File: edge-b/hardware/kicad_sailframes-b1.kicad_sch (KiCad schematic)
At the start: 0 parts

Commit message: B1 schematic Section 8: Battery Monitor (proof of concept)
3 components: R1 (100k), R2 (100k), C1 (100nF). 6 wire stubs, 6 net
labels (VBAT x1, VBAT_DIV x3, GND x2). Verified to open cleanly in
KiCad 10.

Pattern: use Device:R and Device:C from KiCad's standard Device library
(symbol defs copied into the schematic's lib_symbols section), place
each component with a fresh UUID, give each pin a short wire stub to a
named label. Matching labels create electrical connections without
needing junctions or drawn wires between components. ERC will flag
single-occurrence labels until the connecting section is added — e.g.,
VBAT is 1x here, will become 2x when TP4056 BAT pin is added in Section
1.

Library symbol Device:R copied verbatim from edge-e/hardware/kicad_sailframes-e1.kicad_sch
(already at 2-tab indent and named "Device:R"). Library symbol Device:C
copied from KiCad's bundled Device.kicad_sym with +1 tab adjustment and
"C" -> "Device:C" rename on the first line. Both are KiCad-10 format.

Build script lives at /tmp/build_section8.py for reference. Sections 2,
10, 1 will follow the same pattern with components from the project
libraries (B1_MT3608, B1_JLC, etc.) — verifying actual symbol names
before referencing.

Co-Authored-By: Claude Opus 4.7 (1M context) <noreply@anthropic.com>
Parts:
- added C1: 100nF, Capacitor_SMD:C_0603_1608Metric, symbol Device:C
- added R1, R2: 100k, Resistor_SMD:R_0603_1608Metric, symbol Device:R
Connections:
- new net GND: C1.2, R2.2
- new net VBAT: R1.1
- new net VBAT_DIV: C1.1, R1.2, R2.1

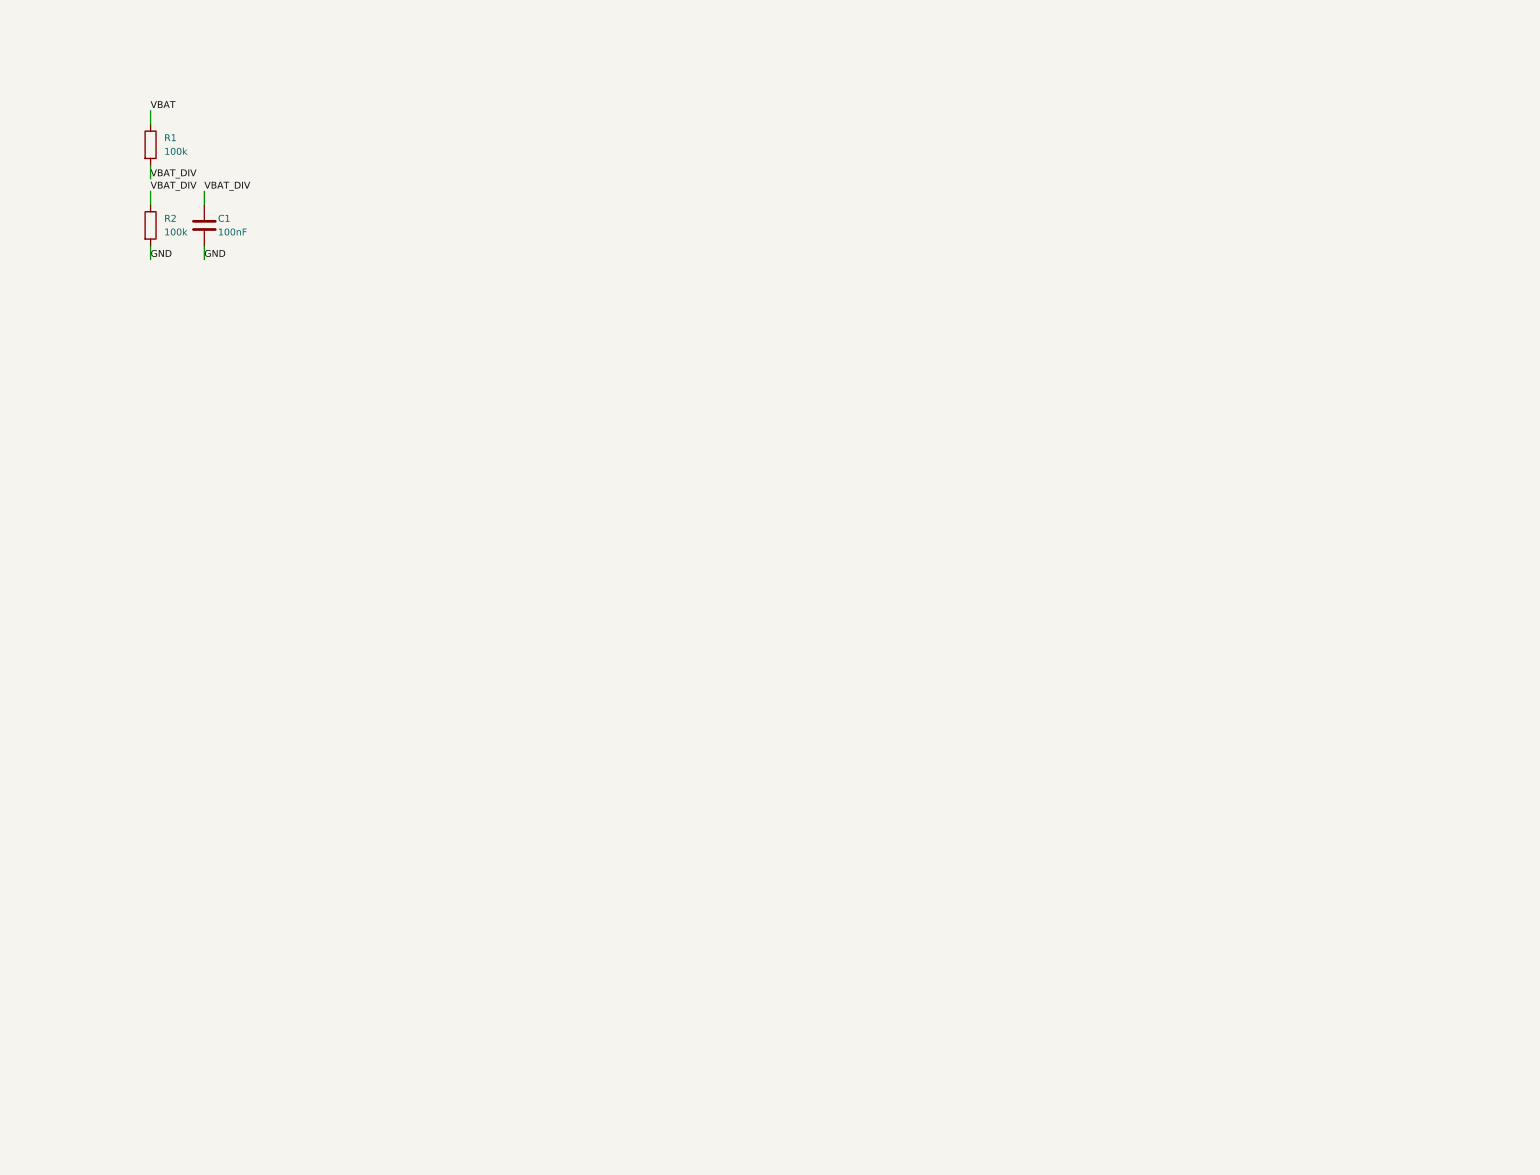
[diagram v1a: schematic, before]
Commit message: B1 schematic Sections 1+2+8+10: power, boost, battery monitor, Hall latch
32 new components + 85 wires + 85 labels added on top of Section 8's
baseline (3 components, 6 wires, 6 labels). Total now 35 / 91 / 91.

Section 1 (Power Input + Charger): U2 TP4056 SOIC-8, D7/D8 SS14 OR-ing
diodes, D2 yellow + D3 green LEDs (CHRG/STDBY indicators) with R8/R9
series 1k, R6 (PROG 2k) and R7 (TEMP 10k), C2/C3 VCC decoupling (10uF +
100nF), C4/C5 BAT decoupling (10uF + 100nF), J2 JST PH for battery,
J_QI 2-pin Qi solder pads.

Section 2 (Boost Converter): U3 MT3608 SOT-23-6, L1 22uH inductor, D9
SS14 boost diode, C7 10uF input cap, C8 22uF output cap, R10/R11 100k
/ 13.3k feedback divider (Vout ~5.11V, can refine to 13.7k for 4.98V).
MT3608 EN pin nets to LATCH_Q (spec checklist line 1259 - the
double-gating requirement). MT3608 NC pin (6) marked no_connect.

Section 10 (Hall Latch / Magnetic Power Switch): U_HALL DRV5032AJ, R12
100k pull-up for open-drain, R13/C9 10k/100nF debounce, U_FF
SN74LVC1G74DCTR SM8 flip-flop in toggle config (D tied to /Q via
FF_D_QBAR label), U_RST MAX809T 3.08V supervisor on /CLR (spec
checklist line 1260 - no RC POR network), R14 10k base resistor, Q_INV
2N3904 NPN level shifter, R15 100k gate pull-up, Q_PWR AO3401A P-MOSFET
switching V5_UNSW to V5_SW. U_HALL pin 3 (NC per symbol) marked
no_connect.

Library additions to lib_symbols (8 new top-level): Device:C, Device:L,
Device:LED, Connector_Generic:Conn_01x02, B1_TP4056:TP4056,
B1_MT3608:MT3608, B1_SS14:SS14, B1_DRV5032AJ:DRV5032AJDMRR,
B1_2N3904:MMBT3904-C20526, B1_AO3401A:AO3401A,
B1_JLC:SN74LVC1G74DCTR, B1_JLC:MAX809T.

Net distribution:
- GND: 22, VBAT: 12 (high-fanout rails)
- TP4056_VCC: 6 (VCC + CE + 2 decoupling caps + OR-diodes' cathodes)
- V5_UNSW: 5, V5_SW: 4 (pre/post Q_PWR MOSFET)
- LATCH_Q: 3 (U_FF.Q + R14 + MT3608.EN - the critical double-gate)
- Internal section nets (HALL_OUT, CLK_DEBOUNCED, FB_MID, etc.): 2-3 each

Verified to load cleanly in KiCad 10 after stripping ; comments (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
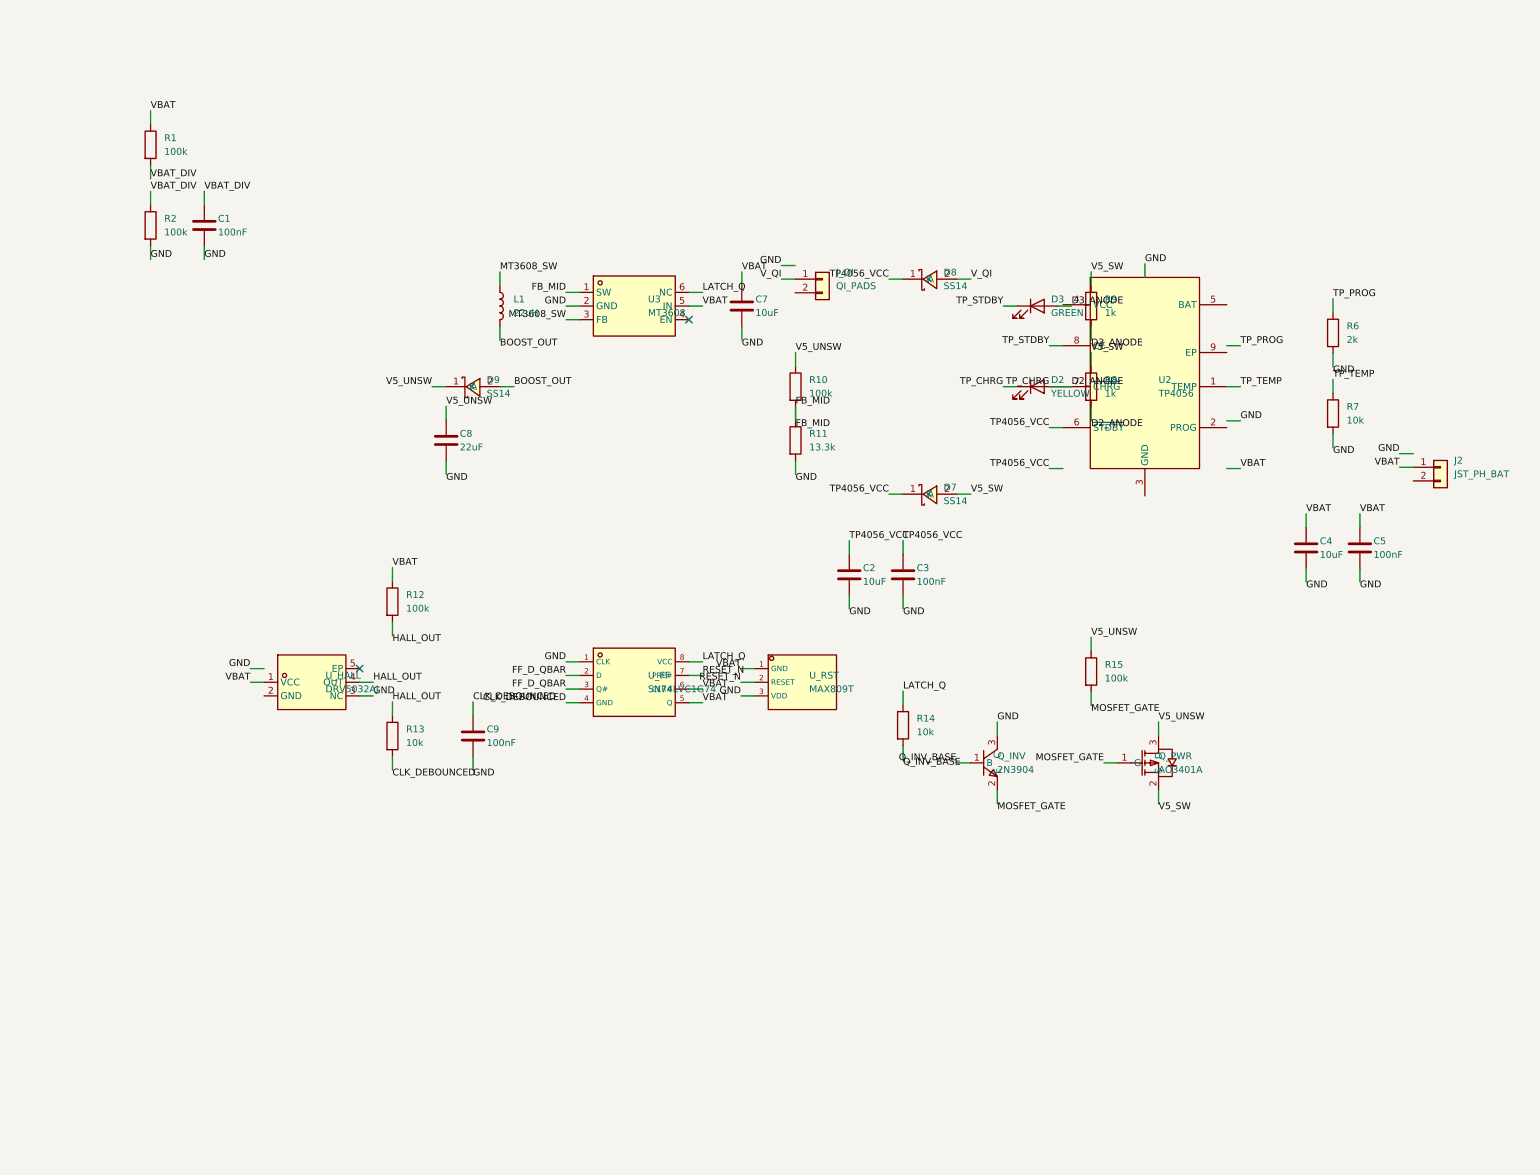
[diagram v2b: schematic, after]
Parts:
- added C2, C4, C7: 10uF, Capacitor_SMD:C_0603_1608Metric, symbol Device:C
- added C3, C5, C9: 100nF, Capacitor_SMD:C_0603_1608Metric, symbol Device:C
- added C8: 22uF, Capacitor_SMD:C_0603_1608Metric, symbol Device:C
- added D2: YELLOW, LED_SMD:LED_0805_2012Metric, symbol Device:LED
- added D3: GREEN, LED_SMD:LED_0805_2012Metric, symbol Device:LED
- added D7, D8, D9: SS14, Diode_SMD:D_SMA, symbol B1_SS14:SS14
- added J2: JST_PH_BAT, Connector_JST:JST_PH_S2B-PH-K_1x02_P2.00mm_Vertical, symbol Connector_Generic:Conn_01x02
- added J_QI: QI_PADS, Connector_PinHeader_2.54mm:PinHeader_1x02_P2.54mm_Vertical, symbol Connector_Generic:Conn_01x02
- added L1: 22uH, Inductor_SMD:L_Bourns_SRR4528, symbol Device:L
- added Q_INV: 2N3904, Package_TO_SOT_SMD:SOT-23, symbol B1_2N3904:MMBT3904-C20526
- added Q_PWR: AO3401A, Package_TO_SOT_SMD:SOT-23, symbol B1_AO3401A:AO3401A
- added R10, R12, R15: 100k, Resistor_SMD:R_0603_1608Metric, symbol Device:R
- added R11: 13.3k, Resistor_SMD:R_0603_1608Metric, symbol Device:R
- added R13, R14, R7: 10k, Resistor_SMD:R_0603_1608Metric, symbol Device:R
- added R6: 2k, Resistor_SMD:R_0603_1608Metric, symbol Device:R
- added R8, R9: 1k, Resistor_SMD:R_0603_1608Metric, symbol Device:R
- added U2: TP4056, Package_SO:SOIC-8_3.9x4.9mm_P1.27mm, symbol B1_TP4056:TP4056
- added U3: MT3608, Package_TO_SOT_SMD:SOT-23-6, symbol B1_MT3608:MT3608
- added U_FF: SN74LVC1G74, Package_SO:SM8, symbol B1_JLC:SN74LVC1G74DCTR
- added U_HALL: DRV5032AJ, Package_DFN_QFN:X2SON-4_1x1mm_P0.5mm, symbol B1_DRV5032AJ:DRV5032AJDMRR
- added U_RST: MAX809T, Package_TO_SOT_SMD:SOT-23, symbol B1_JLC:MAX809T
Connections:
- net GND: now also C2.2, C3.2, C4.2, C5.2, C7.2, C8.2, C9.2, Q_INV.3 (C), R11.2, R6.2, R7.2, U3.2 (GND), U_FF.1 (CLK), U_HALL.3 (NC), U_RST.3 (VDD)
- net VBAT: now also C4.1, C5.1, C7.1, J2.1 (Pin_1), R12.1, U3.5 (IN), U_FF.5 (Q), U_FF.6 (CLR#), U_HALL.1 (VCC), U_RST.1 (GND)
- new net BOOST_OUT: D9.2 (A), L1.2
- new net CLK_DEBOUNCED: C9.1, R13.2, U_FF.4 (GND)
- new net D2_ANODE: D2.1 (K), D2.2 (A), R8.2, U2.7 (~{CHRG})
- new net D3_ANODE: D3.2 (A), R9.2
- new net FB_MID: R10.2, R11.1, U3.1 (SW)
- new net FF_D_QBAR: U_FF.2 (D), U_FF.3 (Q#)
- new net HALL_OUT: R12.2, R13.1, U_HALL.4 (OUT)
- new net LATCH_Q: R14.1, U3.6 (NC), U_FF.8 (VCC)
- new net MOSFET_GATE: Q_INV.2 (E), Q_PWR.1 (G), R15.2
- new net MT3608_SW: L1.1, U3.3 (FB)
- new net Q_INV_BASE: Q_INV.1 (B), R14.2
- new net RESET_N: U_FF.7 (PRE#), U_RST.2 (RESET)
- new net TP4056_VCC: C2.1, C3.1, D7.1 (K), D8.1 (K), U2.6 (~{STDBY})
- new net TP_PROG: R6.1
- new net TP_STDBY: D3.1 (K), U2.8 (CE)
- new net TP_TEMP: R7.1, U2.1 (TEMP)
- new net V5_SW: D7.2 (A), Q_PWR.2 (S), R8.1, R9.1
- new net V5_UNSW: C8.1, D9.1 (K), Q_PWR.3 (D), R10.1, R15.1
- new net V_QI: D8.2 (A), J_QI.1 (Pin_1)
- no-connect marks 0 -> 2

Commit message: B1 schematic ERC cleanup: Y-flip fix, PWR_FLAGs, R11 tuning
Critical bug fix: pin canvas position was computed using sym_y + py
instead of sym_y - py. KiCad symbols use Y-up math convention while
schematic canvas uses Y-down — KiCad inverts Y when placing symbols.
The earlier code missed this. For symmetric components (R, C, L) the
bug only swapped pin 1 with pin 2 — electrically equivalent. For
asymmetric components (TP4056, MT3608, U_FF, U_HALL, ...), wires landed
5–30 mm away from actual pins, leaving 8 pins unconnected.

Fix:
- stub_label() now computes canvas Y as comp_y - py (Y-flip)
- stub_offset() rotations 90 and 270 swapped (pin direction inverts
  with Y axis)
- Section 8 connection data swapped pin 1 ↔ pin 2 to preserve original
  visual (VBAT label above R1, VBAT_DIV between R1↔R2, GND below)

Additional cleanup in this commit:
- 7 PWR_FLAG instances added on each power rail (VBAT, V5_UNSW, V5_SW,
  V_QI, TP4056_VCC, V3V3, GND) — placed in a row at y=30 above
  Section 8. Tells ERC each rail has a declared power source. V3V3
  remains isolated until Section 4 (ESP32 socket) is added.
- R11 (MT3608 feedback bottom) tuned from 13.3k → 13.7k for
  Vout = 0.6 × (1 + 100/13.7) = 4.98 V (target 5.0 V)
- power:PWR_FLAG library symbol copied from E1 schematic into
  lib_symbols

ERC results after fix (kicad-cli):
- pin_not_connected:   8 → 0  ✓ critical fixed
- unconnected_endpoint: 8 → 0  ✓ fixed
- isolated_pin_label:  3 → 1  (V3V3 waits for Section 4)
- pin_to_pin:         33 → 39  (Unspecified/Passive type mismatches,
                                easyeda2kicad symbols — cosmetic)
- footprint_link:     4    (wrong KiCad-standard footprint names —
                            cosmetic)
- endpoint_off_grid:  140  (cosmetic — components not on 1.27 mm grid)

UUIDs all regenerated since the rebuild was full-replace; git diff shows
the entire schematic body as changed but the connection topology is
preserved and visually verified per b1.pdf.

Co-Authored-By: Cla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
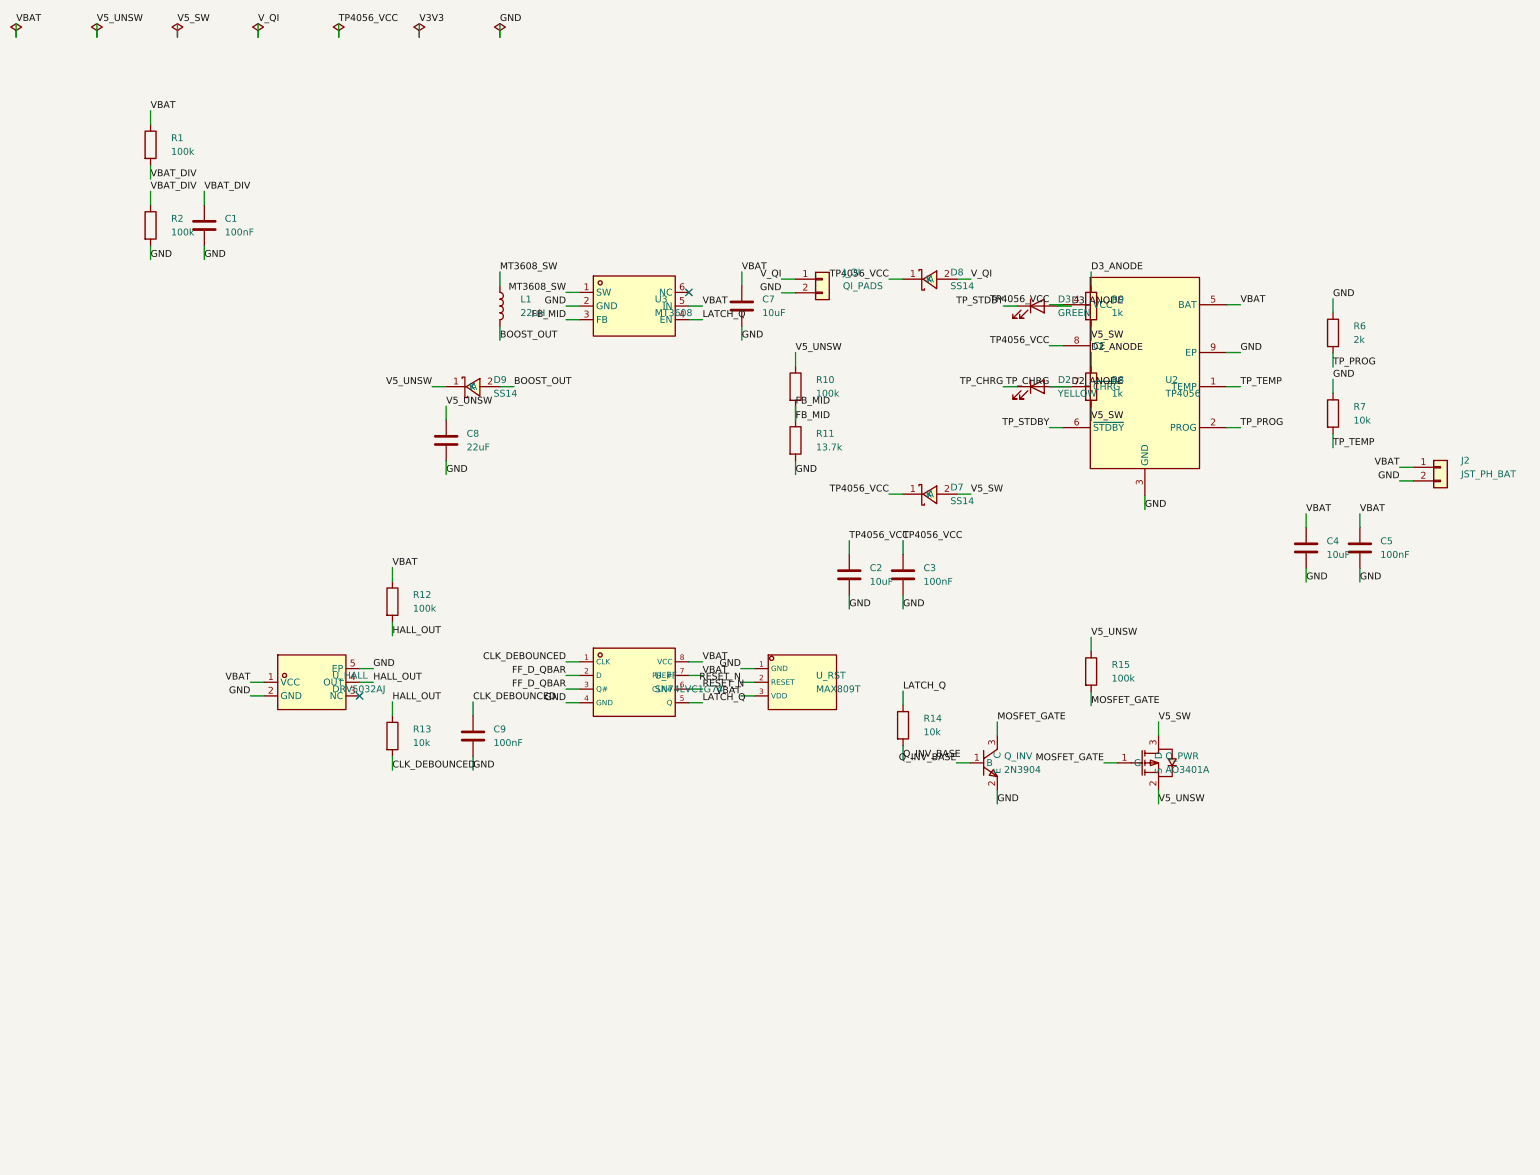
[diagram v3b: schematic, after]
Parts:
- R11: value 13.3k -> 13.7k
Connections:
- net CLK_DEBOUNCED: now also U_FF.1 (CLK); no longer U_FF.4 (GND)
- net D2_ANODE: now also R8.1; no longer R8.2
- net D3_ANODE: now also R9.1; no longer R9.2
- net FB_MID: now also U3.3 (FB); no longer U3.1 (SW)
- net GND: now also J2.2 (Pin_2), J_QI.2 (Pin_2), Q_INV.2 (E), R6.1, R7.1, U2.3 (GND), U2.9 (EP), U_FF.4 (GND), U_HALL.2 (GND), U_HALL.5 (EP), U_RST.1 (GND); no longer Q_INV.3 (C), R6.2, R7.2, U_FF.1 (CLK), U_HALL.3 (NC), U_RST.3 (VDD)
- net LATCH_Q: now also U3.4 (EN), U_FF.5 (Q); no longer U3.6 (NC), U_FF.8 (VCC)
- net MOSFET_GATE: now also Q_INV.3 (C); no longer Q_INV.2 (E)
- net MT3608_SW: now also U3.1 (SW); no longer U3.3 (FB)
- net RESET_N: now also U_FF.6 (CLR#); no longer U_FF.7 (PRE#)
- net TP4056_VCC: now also U2.4 (VCC), U2.8 (CE); no longer U2.6 (~{STDBY})
- net TP_PROG: now also R6.2, U2.2 (PROG); no longer R6.1
- net TP_STDBY: now also U2.6 (~{STDBY}); no longer U2.8 (CE)
- net TP_TEMP: now also R7.2; no longer R7.1
- net V5_SW: now also Q_PWR.3 (D), R8.2, R9.2; no longer Q_PWR.2 (S), R8.1, R9.1
- net V5_UNSW: now also Q_PWR.2 (S); no longer Q_PWR.3 (D)
- net VBAT: now also U2.5 (BAT), U_FF.7 (PRE#), U_FF.8 (VCC), U_RST.3 (VDD); no longer U_FF.5 (Q), U_FF.6 (CLR#), U_RST.1 (GND)
